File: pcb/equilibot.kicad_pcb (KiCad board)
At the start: 4 copper layers, 88.8 x 49.5 mm, 152 parts, among them IC1 TMC5240, IC2 TMC5240, IC3 TPS561243DRLR, IC4 TPS561243DRLR, J1 Conn_01x02_Socket, J2 USB_C_Receptacle_USB2.0_16P, J3 Conn_01x04_Pin, J4 Conn_01x04_Pin, J5 Conn_01x03_Pin, J7 Conn_01x08_Pin, SW1 SW_Push, SW2 SW_Push, U1 ESP32-S3-WROOM-1, U2 SN74LVC1T45DBV, U3 USBLC6-2P6, U4 TLV75533PDBV

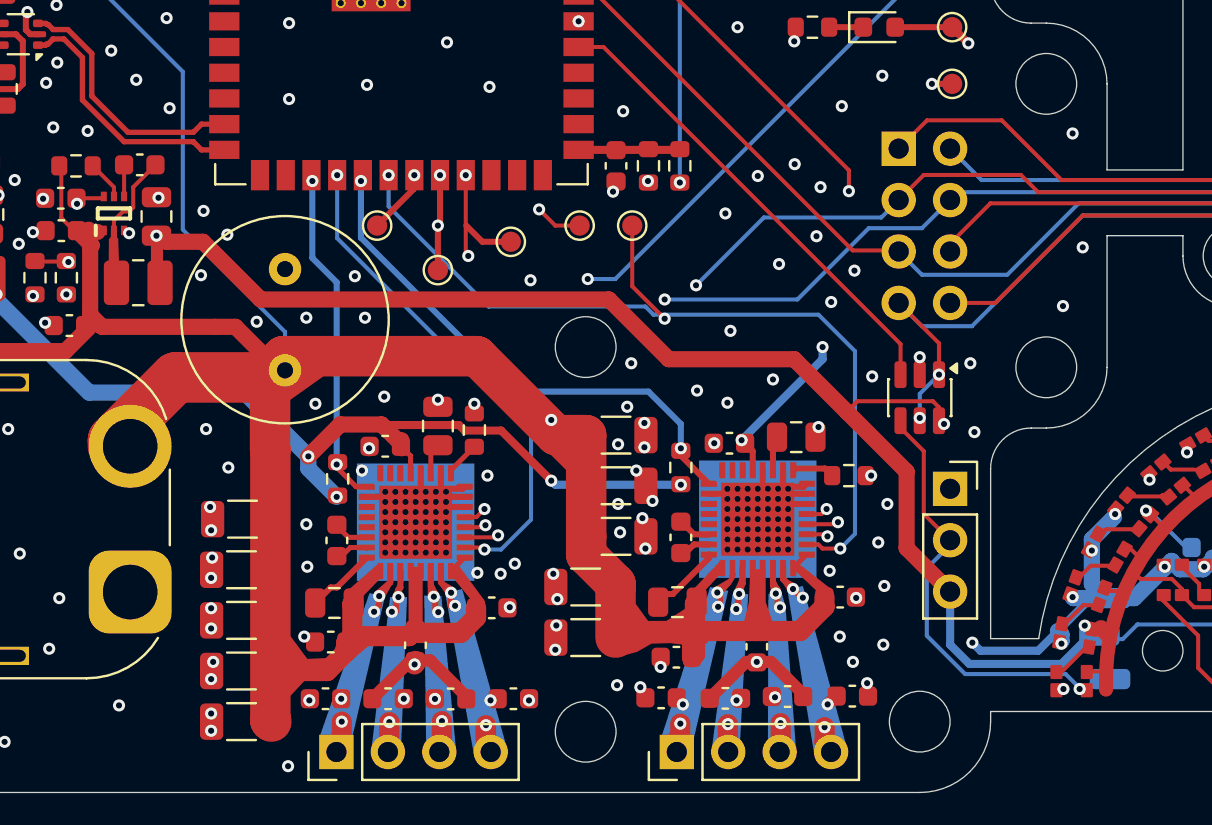
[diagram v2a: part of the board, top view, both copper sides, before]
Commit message: remove esp32 module from production
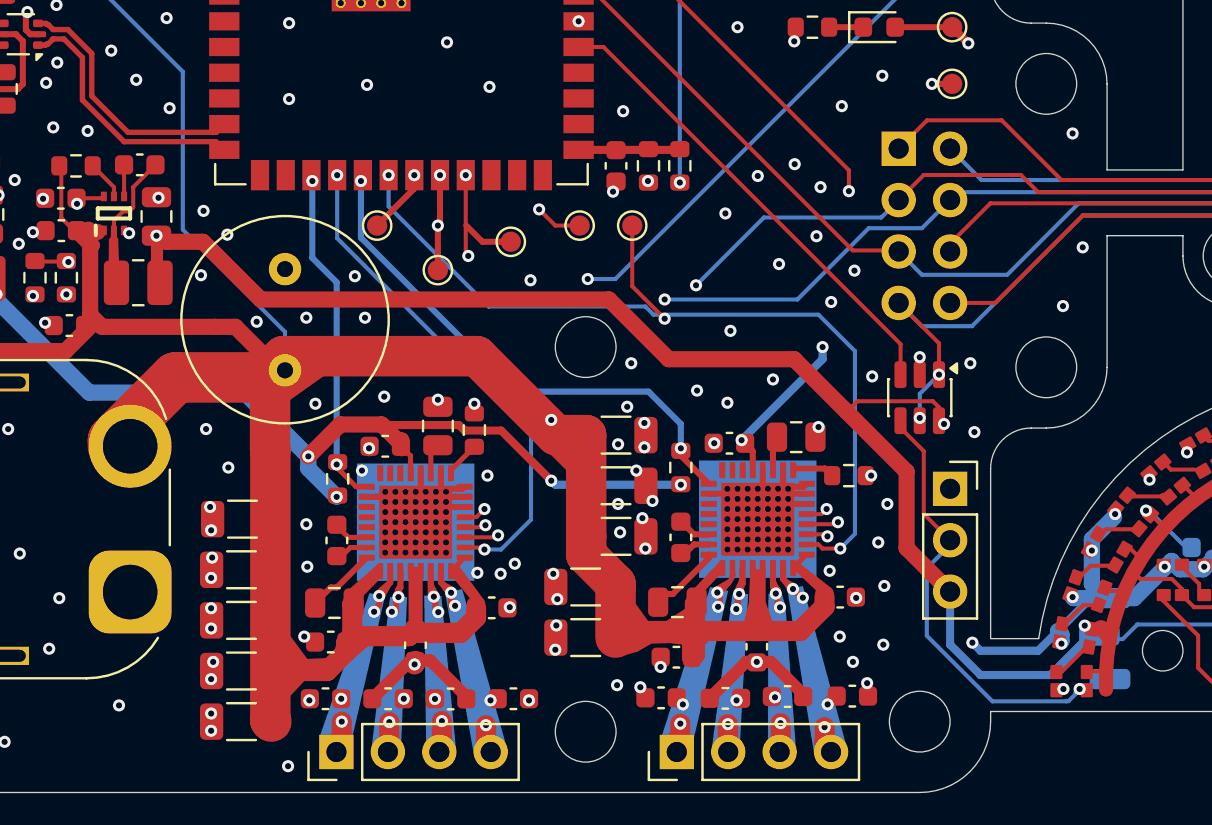
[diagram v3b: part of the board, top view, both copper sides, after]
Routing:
- net /leds/DIN_5V: track 22.2 -> 22.9 mm
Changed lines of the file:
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@@
 		)
 		(pad "2" smd roundrect
-			(at -0.75 0.450001 340)
+			(at -0.75 0.450002 340)
 			(size 0.6 0.7)
 			(layers "F.Cu" "F.Mask" "F.Paste")
@@
 		)
 		(pad "4" smd roundrect
-			(at 0.75 -0.450001 340)
+			(at 0.75 -0.450002 340)
 			(size 0.6 0.7)
 			(layers "F.Cu" "F.Mask" "F.Paste")
@@
 		)
 		(pad "1" smd roundrect
-			(at -0.75 -0.450001 290)
+			(at -0.75 -0.450002 290)
 			(size 0.6 0.7)
 			(layers "F.Cu" "F.Mask" "F.Paste")
@@
 		)
 		(pad "3" smd roundrect
-			(at 0.75 0.450001 290)
+			(at 0.75 0.450002 290)
 			(size 0.6 0.7)
 			(layers "F.Cu" "F.Mask" "F.Paste")
@@
 		)
 		(pad "1" smd roundrect
-			(at -0.75 -0.450001 200)
+			(at -0.75 -0.450002 200)
 			(size 0.6 0.7)
 			(layers "F.Cu" "F.Mask" "F.Paste")
@@
 		)
 		(pad "3" smd roundrect
-			(at 0.75 0.450001 200)
+			(at 0.75 0.450002 200)
 			(size 0.6 0.7)
 			(layers "F.Cu" "F.Mask" "F.Paste")
@@
 		)
 		(pad "2" smd roundrect
-			(at -0.75 0.450001 250)
+			(at -0.75 0.450002 250)
 			(size 0.6 0.7)
 			(layers "F.Cu" "F.Mask" "F.Paste")
@@
 		)
 		(pad "4" smd roundrect
-			(at 0.75 -0.450001 250)
+			(at 0.75 -0.450002 250)
 			(size 0.6 0.7)
 			(layers "F.Cu" "F.Mask" "F.Paste")
@@
 	(gr_poly
 		(pts
-			(xy 149.69 104.91) (xy 150.91 106.05) (xy 151.7 106.01) (xy 149.87 104.58)
+			(xy 149.69 104.91) (xy 150.91 106.05) (xy 151.675 105.935) (xy 149.845 104.505)
 		)
 		(stroke
@@
 	)
 	(segment
-		(start 163 109.65)
-		(end 158.45 109.65)
-		(width 0.4)
-		(layer "B.Cu")
-		(net 2)
-	)
-	(segment
-		(start 165 108.4)
-		(end 164.25 108.4)
+		(start 159 110.2)
+		(end 157.5 108.7)
 		(width 0.4)
 		(layer "B.Cu")
@@
 	)
 	(segment
-		(start 164.25 108.4)
-		(end 163 109.65)
+		(start 157.5 108.7)
+		(end 157.5 106.08)
 		(width 0.4)
 		(layer "B.Cu")
@@
 	)
 	(segment
-		(start 157.5 108.7)
-		(end 157.5 106.08)
+		(start 165 108.4)
+		(end 164.25 108.4)
 		(width 0.4)
 		(layer "B.Cu")
@@
 	)
 	(segment
-		(start 158.45 109.65)
-		(end 157.5 108.7)
-		(width 0.4)
-		(layer "B.Cu")
-		(net 2)
-	)
-	(segment
 		(start 182.775 101.5)
 		(end 182.775 100.325)
@@
 	)
 	(segment
+		(start 162.45 110.2)
+		(end 159 110.2)
+		(width 0.4)
+		(layer "B.Cu")
+		(net 2)
+	)
+	(segment
 		(start 182.775 100.325)
 		(end 183.175 99.925)
@@
 	)
 	(segment
+		(start 164.25 108.4)
+		(end 162.45 110.2)
+		(width 0.4)
+		(layer "B.Cu")
+		(net 2)
+	)
+	(segment
 		(start 176.95 103.55)
 		(end 176.95 101.2)
@@
 	)
 	(segment
-		(start 156.349 108.257521)
-		(end 156.349 104.926)
+		(start 163.897043 110.888502)
+		(end 163.897043 110.839737)
+		(width 0.2)
+		(layer "B.Cu")
+		(net 3)
+	)
+	(segment
+		(start 156.349 104.926)
+		(end 157.5 103.775)
+		(width 0.2)
+		(layer "B.Cu")
+		(net 3)
+	)
+	(segment
+		(start 163.698041 111.138621)
+		(end 163.345984 111.490678)
+		(width 0.2)
+		(layer "B.Cu")
+		(net 3)
+	)
+	(segment
+		(start 163.246102 111.490678)
+		(end 163.23678 111.5)
+		(width 0.2)
+		(layer "B.Cu")
+		(net 3)
+	)
+	(segment
+		(start 163.897043 110.839737)
+		(end 163.698041 111.038739)
 		(width 0.2)
 		(layer "B.Cu")
@@
 	)
 	(segment
-		(start 158.242479 110.151)
-		(end 156.349 108.257521)
+		(start 163.698041 111.038739)
+		(end 163.698041 111.138621)
 		(width 0.2)
 		(layer "B.Cu")
@@
 	)
 	(segment
-		(start 163.208306 110.151)
-		(end 158.242479 110.151)
+		(start 156.349 108.257521)
+		(end 156.349 104.926)
 		(width 0.2)
 		(layer "B.Cu")
@@
 	)
 	(segment
-		(start 163.897043 110.888502)
-		(end 163.897043 110.839737)
+		(start 163.345984 111.490678)
+		(end 163.246102 111.490678)
 		(width 0.2)
 		(layer "B.Cu")
@@
 	)
 	(segment
-		(start 156.349 104.926)
-		(end 157.5 103.775)
+		(start 159.591479 111.5)
+		(end 156.349 108.257521)
 		(width 0.2)
 		(layer "B.Cu")
@@
 	)
 	(segment
-		(start 163.897043 110.839737)
-		(end 163.208306 110.151)
+		(start 164.211498 110.888502)
+		(end 164.7 110.4)
 		(width 0.2)
 		(layer "B.Cu")
@@
 	)
 	(segment
-		(start 164.211498 110.888502)
-		(end 164.7 110.4)
+		(start 163.23678 111.5)
+		(end 159.591479 111.5)
 		(width 0.2)
 		(layer "B.Cu")
@@
 	)
 	(segment
-		(start 113.1832 78.30384)
-		(end 113.1832 78.3178)
+		(start 113.1832 78.3178)
+		(end 113.921182 78.3178)
 		(width 0.2644)
 		(layer "F.Cu")
@@
 	)
 	(segment
-		(start 112.45 78.0125)
-		(end 112.825001 78.0125)
+		(start 121.65 83)
+		(end 121.65 82.99)
 		(width 0.2644)
 		(layer "F.Cu")
@@
 	)
 	(segment
-		(start 113.921182 78.3178)
-		(end 115.1072 79.503818)
+		(start 113.1832 78.30384)
+		(end 113.1832 78.3178)
 		(width 0.2644)
 		(layer "F.Cu")
@@
 	)
 	(segment
-		(start 112.879301 78.0668)
-		(end 112.94616 78.0668)
+		(start 121.2572 83.3928)
+		(end 121.65 83)
 		(width 0.2644)
 		(layer "F.Cu")
@@
 	)
 	(segment
-		(start 112.94616 78.0668)
-		(end 113.1832 78.30384)
+		(start 116.896182 83.3928)
+		(end 121.2572 83.3928)
 		(width 0.2644)
 		(layer "F.Cu")
@@
 	)
 	(segment
-		(start 120.122199 83.3928)
-		(end 120.524999 82.99)
+		(start 115.1072 79.503818)
+		(end 115.1072 81.603818)
 		(width 0.2644)
 		(layer "F.Cu")
@@
 	)
 	(segment
-		(start 120.524999 82.99)
-		(end 121.65 82.99)
+		(start 112.45 78.0125)
+		(end 112.825001 78.0125)
 		(width 0.2644)
 		(layer "F.Cu")
@@
 	)
 	(segment
-		(start 115.1072 79.503818)
-		(end 115.1072 81.603818)
+		(start 112.94616 78.0668)
+		(end 113.1832 78.30384)
 		(width 0.2644)
 		(layer "F.Cu")
@@
 	)
 	(segment
-		(start 115.1072 81.603818)
-		(end 116.896182 83.3928)
+		(start 113.921182 78.3178)
+		(end 115.1072 79.503818)
 		(width 0.2644)
 		(layer "F.Cu")
@@
 	)
 	(segment
-		(start 113.1832 78.3178)
-		(end 113.921182 78.3178)
+		(start 112.879301 78.0668)
+		(end 112.94616 78.0668)
 		(width 0.2644)
 		(layer "F.Cu")
@@
 	)
 	(segment
-		(start 116.896182 83.3928)
-		(end 120.122199 83.3928)
+		(start 115.1072 81.603818)
+		(end 116.896182 83.3928)
 		(width 0.2644)
 		(layer "F.Cu")
@@
 	)
 	(segment
-		(start 112.94616 79.0332)
-		(end 113.1832 78.79616)
+		(start 114.6428 79.696182)
+		(end 114.6428 81.796182)
 		(width 0.2644)
 		(layer "F.Cu")
@@
 	)
 	(segment
-		(start 113.728818 78.7822)
-		(end 114.6428 79.696182)
+		(start 113.1832 78.7822)
+		(end 113.728818 78.7822)
 		(width 0.2644)
 		(layer "F.Cu")
@@
 	)
 	(segment
-		(start 113.1832 78.7822)
-		(end 113.728818 78.7822)
+		(start 112.94616 79.0332)
+		(end 113.1832 78.79616)
 		(width 0.2644)
 		(layer "F.Cu")
@@
 	)
 	(segment
-		(start 120.524999 84.26)
-		(end 121.65 84.26)
+		(start 121.2322 83.8572)
+		(end 121.635 84.26)
 		(width 0.2644)
 		(layer "F.Cu")
@@
 	)
 	(segment
-		(start 112.45 79.0875)
-		(end 112.825001 79.0875)
+		(start 114.6428 81.796182)
+		(end 116.703818 83.8572)
 		(width 0.2644)
 		(layer "F.Cu")
@@
 	)
 	(segment
-		(start 114.6428 79.696182)
-		(end 114.6428 81.796182)
+		(start 112.45 79.0875)
+		(end 112.825001 79.0875)
 		(width 0.2644)
 		(layer "F.Cu")
@@
 	)
 	(segment
-		(start 114.6428 81.796182)
-		(end 116.703818 83.8572)
+		(start 113.728818 78.7822)
+		(end 114.6428 79.696182)
 		(width 0.2644)
 		(layer "F.Cu")
@@
 	)
 	(segment
-		(start 113.1832 78.79616)
-		(end 113.1832 78.7822)
+		(start 121.635 84.26)
+		(end 121.65 84.26)
 		(width 0.2644)
 		(layer "F.Cu")
@@
 	)
 	(segment
-		(start 120.122199 83.8572)
-		(end 120.524999 84.26)
+		(start 116.703818 83.8572)
+		(end 121.2322 83.8572)
 		(width 0.2644)
 		(layer "F.Cu")
@@
 	)
 	(segment
-		(start 116.703818 83.8572)
-		(end 120.122199 83.8572)
+		(start 113.1832 78.79616)
+		(end 113.1832 78.7822)
 		(width 0.2644)
 		(layer "F.Cu")

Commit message: change layout of extern led board to not show vias
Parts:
- J1: footprint Connector_AMASS:AMASS_XT60PW-M_1x02_P7.20mm_Horizontal -> Equilibot:AMASS_XT60PW-M_1x02_P7.20mm_Horizontal
- moved TP11 13.2 mm to (177.6, 104.8), turned to 0 degrees
- moved TP16 12.3 mm to (177.3, 107.4), turned to 0 degrees
- moved TP8 12.2 mm to (176.6, 101.5), turned to 0 degrees
- moved C42 5.31 mm to (181.1, 107.5), turned to 180 degrees
- moved C48 3.04 mm to (167.3, 103.0), turned to 90 degrees
- moved C40 2.72 mm to (184.7, 101.9), turned to 90 degrees
- moved C39 2.27 mm to (172.6, 107.4), turned to 0 degrees
- moved C41 2.26 mm to (176.9, 98.8), turned to 90 degrees
- moved J1 0.53 mm to (116.7, 106.5)
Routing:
- net /leds/DIN_5V: track 22.9 -> 35.8 mm
- net /5V: track 175.0 -> 163.8 mm, vias 12 -> 36
- net /VM: track 186.3 -> 194.0 mm, vias 6 -> 8
- net GND: track 94.0 -> 87.2 mm
- net Net-(D8-DOUT): track 1.63 -> 2.23 mm
- net Net-(D7-DOUT): track 1.60 -> 2.13 mm
- net Net-(D19-DOUT): track 9.09 -> 8.71 mm, vias 0 -> 2
- net Net-(D27-DOUT): track 3.38 -> 3.75 mm, vias 0 -> 2
- net /leds/O2: track 6.18 -> 6.47 mm, vias 0 -> 2
- net Net-(D28-DOUT): track 4.92 -> 5.11 mm, vias 0 -> 2
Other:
- outline, holes or cut-outs redrawn
